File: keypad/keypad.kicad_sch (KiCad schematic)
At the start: 55 parts, among them P1 USB_C_Plug_USB2.0, SW1 SW_MEC_5E, SW2 SW_MEC_5E, SW3 SW_DIP_x01, SW4 SW_Push, SW5 SW_Push, SW6 SW_Push, U1 RP2040, U2 74HCT245, U3 W25Q16JVUXIQ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

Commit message: Finish RGB and start power
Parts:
- removed SW2: SW_MEC_5E, Button_Switch_THT:SW_Push_2P1T_Toggle_CK_PVA1xxH1xxxxxxV2, symbol Switch:SW_MEC_5E
- removed SW6: SW_Push, Button_Switch_Keyboard:SW_Cherry_MX_1.00u_PCB, symbol Switch:SW_Push
- removed U7: DRV5033AJxDBZ, Package_TO_SOT_SMD:SOT-23, symbol Sensor_Magnetic:DRV5033AJxDBZ
- added D7, D8, D9: WS2812B, LED_SMD:LED_WS2812B_PLCC4_5.0x5.0mm_P3.2mm, symbol LED:WS2812B
- added SW2: SW_MEC_5E, Button_Switch_SMD:SW_Push_1P1T_NO_6x6mm_H9.5mm, symbol Switch:SW_Push
- C3, C4: value 27 pF -> 10 pF
- SW1: footprint Button_Switch_THT:SW_Push_2P1T_Toggle_CK_PVA1xxH1xxxxxxV2 -> Button_Switch_SMD:SW_Push_1P1T_NO_6x6mm_H9.5mm; symbol Switch:SW_MEC_5E -> Switch:SW_Push
- SW3: footprint Button_Switch_SMD:SW_DIP_SPSTx01_Slide_9.78x4.72mm_W8.61mm_P2.54mm -> Jumper:SolderJumper-2_P1.3mm_Open_Pad1.0x1.5mm
- Y1: value ABLS-12.000MHz-B4-T -> ABM8G-12.000MHZ-4Y-T3; footprint Crystal:Crystal_HC18-U_Vertical -> Crystal:Crystal_SMD_Abracon_ABM8G-4Pin_3.2x2.5mm; symbol Device:Crystal -> Device:Crystal_GND24
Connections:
- net +3.3V: now also SW1.2, SW2.2; no longer C21.1, SW1.4 (A)
- net AUX0: now also U1.29 (GPIO18); no longer U1.6 (GPIO4)
- net AUX1: now also U1.30 (GPIO19); no longer U1.7 (GPIO5)
- net GND: now also Y1.2, Y1.4, D7.3 (VSS), D8.3 (VSS), D9.3 (VSS)
- net RGB_D0: now also U1.28 (GPIO17); no longer U1.12 (GPIO9)
- net VBUS: now also D7.1 (VDD), D8.1 (VDD), D9.1 (VDD)
- net at C5.1, C6.1, U1.23 (DVDD)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: now also C21.1
- net at C3.2, U1.20 (XIN): now also Y1.3; no longer Y1.2
- net at R2.2, R4.1: now also SW2.1
- net at D5.2 (DOUT): now also D7.4 (DIN)
- net ADC2: no longer names the net of U1.40 (GPIO28_ADC2)
- new net: D8.2 (DOUT), D9.4 (DIN)
- new net: D7.2 (DOUT), D8.4 (DIN)
- no-connect marks 51 -> 46
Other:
- moved on the sheet: C13, C15, C5, C6, C8, D1, D2, D3, D4, D5, SW4, SW5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

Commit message: finish placing everything
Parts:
- added C22: 100n, Capacitor_SMD:C_0805_2012Metric, symbol Device:C
- added J1: Conn_01x02_Male, Connector_PinHeader_1.27mm:PinHeader_1x02_P1.27mm_Vertical, symbol Connector:Conn_01x02_Male
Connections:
- net +3.3V: now also C22.1; no longer C7.1, U1.43 (ADC_AVDD)
- net ADC_AVDD: now also C7.1, U1.43 (ADC_AVDD)
- net GND: now also C22.2
- net at U1.24 (SWCLK): now also J1.1 (Pin_1)
- net at U1.25 (SWD): now also J1.2 (Pin_2)
- no-connect marks 46 -> 44
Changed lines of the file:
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@@
   (junction (at 185.42 233.68) (diameter 0) (color 0 0 0 0)
   )
+  (junction (at 203.2 53.34) (diameter 0) (color 0 0 0 0)
+  )
   (junction (at 107.95 71.12) (diameter 0) (color 0 0 0 0)
   )
@@
   )
   (junction (at 85.09 146.05) (diameter 0) (color 0 0 0 0)
-  )
-  (junction (at 151.13 63.5) (diameter 0) (color 0 0 0 0)
   )
   (junction (at 185.42 213.36) (diameter 0) (color 0 0 0 0)
@@
   (no_connect (at 125.73 218.44))
   (no_connect (at 377.19 212.09))
-  (no_connect (at 111.76 156.21))
   (no_connect (at 162.56 148.59))
   (no_connect (at 151.13 231.14))
@@
   (no_connect (at 162.56 110.49))
   (no_connect (at 382.27 212.09))
-  (no_connect (at 111.76 158.75))
   (no_connect (at 162.56 92.71))
   (no_connect (at 162.56 130.81))
@@
     (stroke (width 0) (type default) (color 0 0 0 0))
   )
+  (wire (pts (xy 104.14 162.56) (xy 106.68 162.56))
+    (stroke (width 0) (type default) (color 0 0 0 0))
+  )
   (wire (pts (xy 73.66 212.09) (xy 73.66 214.63))
     (stroke (width 0) (type default) (color 0 0 0 0))
@@
     (stroke (width 0) (type default) (color 0 0 0 0))
   )
+  (wire (pts (xy 203.2 53.34) (xy 217.17 53.34))
+    (stroke (width 0) (type default) (color 0 0 0 0))
+  )
   (wire (pts (xy 330.2 213.36) (xy 306.07 213.36))
     (stroke (width 0) (type default) (color 0 0 0 0))
@@
     (stroke (width 0) (type default) (color 0 0 0 0))
   )
+  (wire (pts (xy 106.68 162.56) (xy 106.68 158.75))
+    (stroke (width 0) (type default) (color 0 0 0 0))
+  )
   (wire (pts (xy 175.26 53.34) (xy 189.23 53.34))
     (stroke (width 0) (type default) (color 0 0 0 0))
@@
     (stroke (width 0) (type default) (color 0 0 0 0))
   )
+  (wire (pts (xy 104.14 156.21) (xy 111.76 156.21))
+    (stroke (width 0) (type default) (color 0 0 0 0))
+  )
   (wire (pts (xy 99.06 153.67) (xy 105.41 153.67))
     (stroke (width 0) (type default) (color 0 0 0 0))
@@
     (stroke (width 0) (type default) (color 0 0 0 0))
   )
+  (wire (pts (xy 106.68 158.75) (xy 111.76 158.75))
+    (stroke (width 0) (type default) (color 0 0 0 0))
+  )
   (wire (pts (xy 73.66 135.89) (xy 71.12 135.89))
     (stroke (width 0) (type default) (color 0 0 0 0))
@@
   )
   (wire (pts (xy 60.96 201.93) (xy 63.5 201.93))
+    (stroke (width 0) (type default) (color 0 0 0 0))
+  )
+  (wire (pts (xy 104.14 160.02) (xy 104.14 156.21))
     (stroke (width 0) (type default) (color 0 0 0 0))
   )
@@
     )
   )
+  (global_label "ADC_AVDD" (shape input) (at 144.78 63.5 90) (fields_autoplaced)
+    (effects (font (size 1.27 1.27)) (justify left))
+    (property "Intersheet References" "${INTERSHEET_REFS}" (id 0) (at 144.8594 51.7736 90)
+      (effects (font (size 1.27 1.27)) (justify left) hide)
+    )
+  )
   (global_label "QSPI_SD0" (shape input) (at 111.76 113.03 180) (fields_autoplaced)
     (effects (font (size 1.27 1.27)) (justify right))
@@
     )
     (pin "1")
+  )
+  (symbol (lib_id "Connector:Conn_01x02_Male") (at 99.06 160.02 0) (unit 1)
+    (in_bom yes) (on_board yes) (fields_autoplaced)
+    (property "Reference" "J1" (id 0) (at 99.695 154.94 0))
+    (property "Value" "Conn_01x02_Male" (id 1) (at 99.695 157.48 0))
+    (property "Footprint" "Connector_PinHeader_1.27mm:PinHeader_1x02_P1.27mm_Vertical" (id 2) (at 99.06 160.02 0)
+      (effects (font (size 1.27 1.27)) hide)
+    )
+    (property "Datasheet" "~" (id 3) (at 99.06 160.02 0)
+      (effects (font (size 1.27 1.27)) hide)
+    )
+    (pin "1")
+    (pin "2")
   )
   (symbol (lib_id "power:+3.3V") (at 95.25 201.93 0) (unit 1)
@@
     (pin "2")
   )
+  (symbol (lib_id "power:GND") (at 217.17 60.96 0) (unit 1)
+    (in_bom yes) (on_board yes) (fields_autoplaced)
+    (property "Reference" "#PWR0105" (id 0) (at 217.17 67.31 0)
+      (effects (font (size 1.27 1.27)) hide)
+    )
+    (property "Value" "GND" (id 1) (at 217.17 66.04 0))
+    (property "Footprint" "" (id 2) (at 217.17 60.96 0)
+      (effects (font (size 1.27 1.27)) hide)
+    )
+    (property "Datasheet" "" (id 3) (at 217.17 60.96 0)
+      (effects (font (size 1.27 1.27)) hide)
+    )
+    (pin "1")
+  )
   (symbol (lib_id "LED:WS2812B") (at 306.07 223.52 0) (unit 1)
     (in_bom yes) (on_board yes) (fields_autoplaced)
@@
     (pin "1")
     (pin "2")
-  )
-  (symbol (lib_id "power:+3.3V") (at 151.13 63.5 0) (unit 1)
-    (in_bom yes) (on_board yes) (fields_autoplaced)
-    (property "Reference" "#PWR011" (id 0) (at 151.13 67.31 0)
-      (effects (font (size 1.27 1.27)) hide)
-    )
-    (property "Value" "+3.3V" (id 1) (at 151.13 58.42 0))
-    (property "Footprint" "" (id 2) (at 151.13 63.5 0)
-      (effects (font (size 1.27 1.27)) hide)
-    )
-    (property "Datasheet" "" (id 3) (at 151.13 63.5 0)
-      (effects (font (size 1.27 1.27)) hide)
-    )
-    (pin "1")
   )
   (symbol (lib_id "power:VBUS") (at 153.67 196.85 0) (unit 1)
@@
     (pin "1")
   )
+  (symbol (lib_id "Device:C") (at 217.17 57.15 0) (unit 1)
+    (in_bom yes) (on_board yes) (fields_autoplaced)
+    (property "Reference" "C22" (id 0) (at 220.98 55.8799 0)
+      (effects (font (size 1.27 1.27)) (justify left))
+    )
+    (property "Value" "100n" (id 1) (at 220.98 58.4199 0)
+      (effects (font (size 1.27 1.27)) (justify left))
+    )
+    (property "Footprint" "Capacitor_SMD:C_0805_2012Metric" (id 2) (at 218.1352 60.96 0)
+      (effects (font (size 1.27 1.27)) hide)
+    )
+    (property "Datasheet" "~" (id 3) (at 217.17 57.15 0)
+      (effects (font (size 1.27 1.27)) hide)
+    )
+    (pin "1")
+    (pin "2")
+  )
   (symbol (lib_id "Memory_Flash:W25Q128JVS") (at 241.3 154.94 0) (unit 1)
     (in_bom yes) (on_board yes) (fields_autoplaced)
@@
       (reference "#PWR010") (unit 1) (value "GND") (footprint "")
     )
-    (path "/23cc3252-ed8c-45cf-a713-782ec5caed06"
-      (reference "#PWR011") (unit 1) (value "+3.3V") (footprint "")
-    )
     (path "/8eb3de26-1785-4ce6-9eea-d7c5a25d46d7"
       (reference "#PWR012") (unit 1) (value "GND") (footprint "")
@@
       (reference "#PWR0104") (unit 1) (value "+3.3V") (footprint "")
     )
+    (path "/15c1f430-c43e-49de-8952-ebfdd7bc920c"
+      (reference "#PWR0105") (unit 1) (value "GND") (footprint "")
+    )
     (path "/34b4b529-e4df-4286-a018-6816c646e656"
       (reference "C1") (unit 1) (value "10u") (footprint "Capacitor_SMD:C_0805_2012Metric")
@@
       (reference "C21") (unit 1) (value "100n") (footprint "Capacitor_SMD:C_0805_2012Metric")
     )
+    (path "/de4da200-f592-40f0-ab93-f2fa8fe75a9d"
+      (reference "C22") (unit 1) (value "100n") (footprint "Capacitor_SMD:C_0805_2012Metric")
+    )
     (path "/6a00ced7-1c3c-4889-9134-cc26d1227900"
       (reference "D1") (unit 1) (value "WS2812B") (footprint "LED_SMD:LED_WS2812B_PLCC4_5.0x5.0mm_P3.2mm")
@@
       (reference "D9") (unit 1) (value "WS2812B") (footprint "LED_SMD:LED_WS2812B_PLCC4_5.0x5.0mm_P3.2mm")
     )
+    (path "/02de3128-fb16-4162-a5b1-0ab2657c91ec"
+      (reference "J1") (unit 1) (value "Conn_01x02_Male") (footprint "Connector_PinHeader_1.27mm:PinHeader_1x02_P1.27mm_Vertical")
+    )
     (path "/e71c45d6-c81d-4298-b2c4-54f273ae81a6"

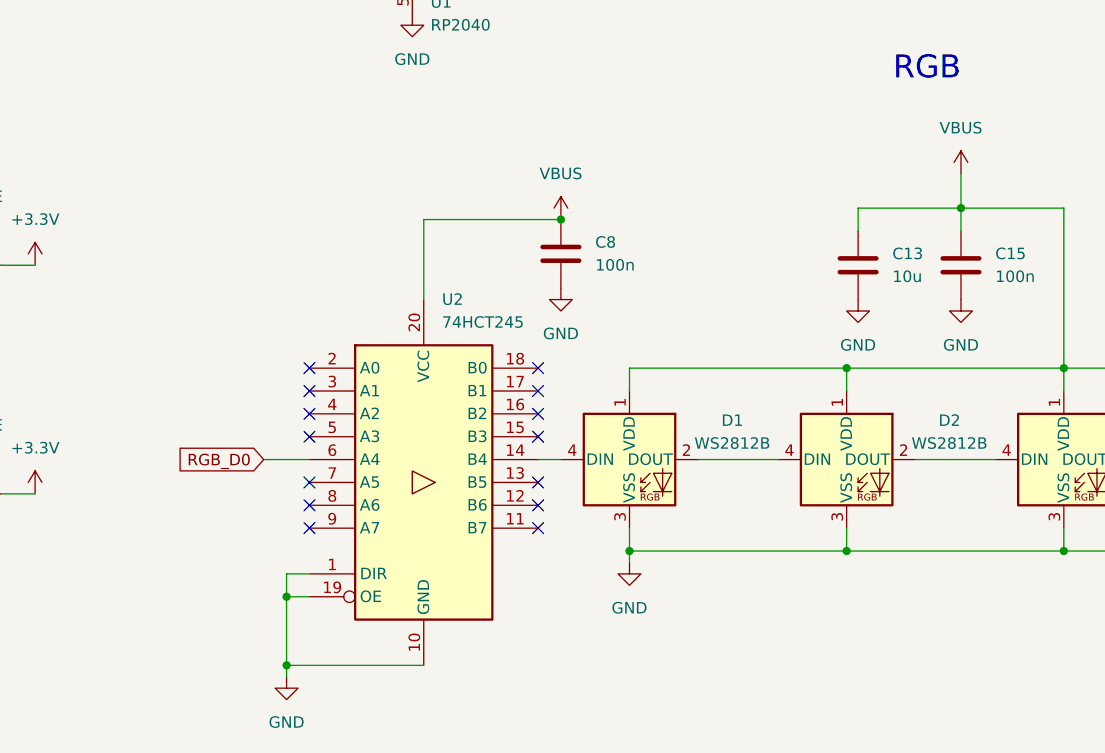
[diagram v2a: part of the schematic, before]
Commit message: Rewire RGB to add space for screwholes
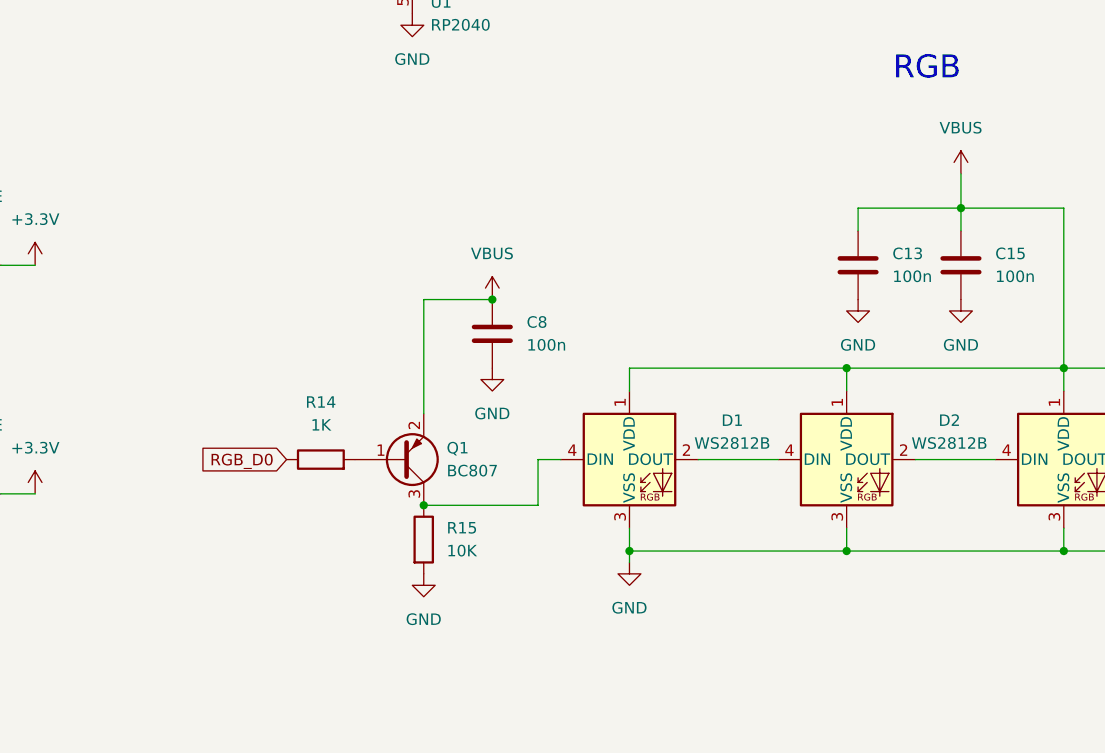
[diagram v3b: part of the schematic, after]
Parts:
- removed U2: 74HCT245, Package_SO:TSSOP-20_4.4x6.5mm_P0.65mm, symbol Custom_Parts:74HCT245
- added Q1: BC807, Package_TO_SOT_SMD:SOT-23, symbol Transistor_BJT:BC807
- added R14: 1K, Resistor_SMD:R_0805_2012Metric, symbol Device:R
- added R15: 10K, Resistor_SMD:R_0805_2012Metric, symbol Device:R
- C13: value 10u -> 100n
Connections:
- net GND: now also R15.2
- net RGB_D0: now also R14.1
- net VBUS: now also Q1.2 (E)
- net at D1.4 (DIN): now also Q1.3 (C), R15.1
- new net: Q1.1 (B), R14.2
- no-connect marks 44 -> 30
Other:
- moved on the sheet: C8

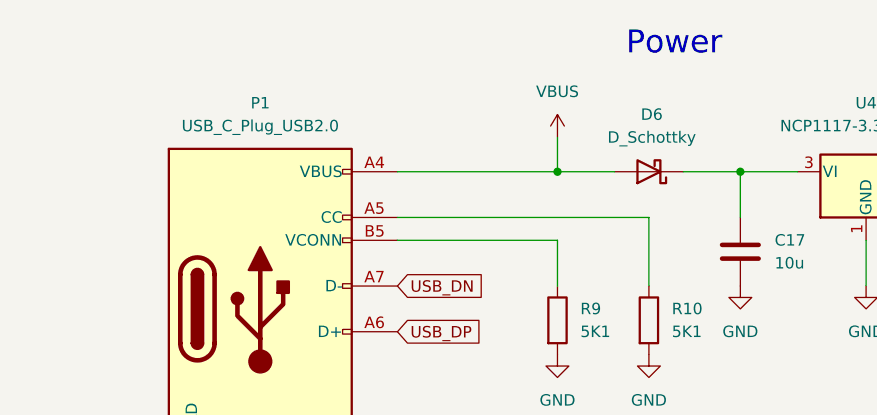
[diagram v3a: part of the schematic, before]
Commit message: Re-spec USB-C and power diode
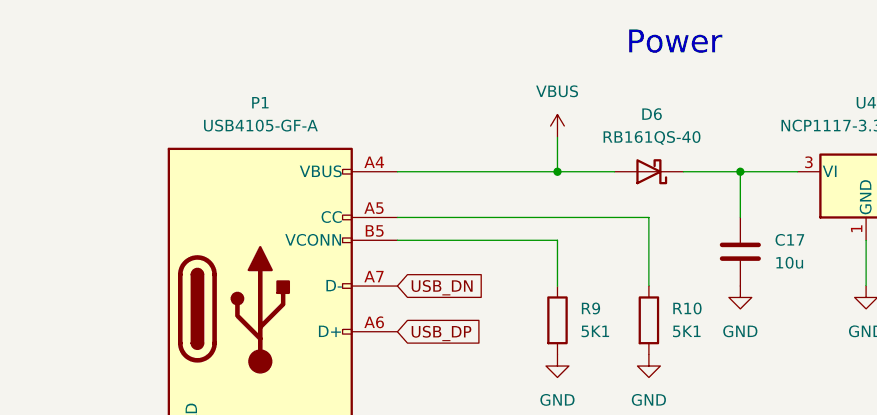
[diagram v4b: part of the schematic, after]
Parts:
- D6: value D_Schottky -> RB161QS-40; footprint Diode_SMD:D_1812_4532Metric -> Diode_SMD:D_0402_1005Metric
- P1: value USB_C_Plug_USB2.0 -> USB4105-GF-A; footprint Connector_USB:USB_C_Receptacle_CNCTech_C-ARA1-AK51X -> Connector_USB:USB_C_Receptacle_GCT_USB4105-xx-A_16P_TopMnt_Horizontal
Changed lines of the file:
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@@
     (in_bom yes) (on_board yes) (fields_autoplaced)
     (property "Reference" "D6" (id 0) (at 300.0375 43.18 0))
-    (property "Value" "D_Schottky" (id 1) (at 300.0375 45.72 0))
-    (property "Footprint" "Diode_SMD:D_1812_4532Metric" (id 2) (at 299.72 49.53 0)
+    (property "Value" "RB161QS-40" (id 1) (at 300.0375 45.72 0))
+    (property "Footprint" "Diode_SMD:D_0402_1005Metric" (id 2) (at 299.72 49.53 0)
       (effects (font (size 1.27 1.27)) hide)
     )
@@
     (in_bom yes) (on_board yes) (fields_autoplaced)
     (property "Reference" "P1" (id 0) (at 256.54 41.91 0))
-    (property "Value" "USB_C_Plug_USB2.0" (id 1) (at 256.54 44.45 0))
-    (property "Footprint" "Connector_USB:USB_C_Receptacle_CNCTech_C-ARA1-AK51X" (id 2) (at 260.35 64.77 0)
+    (property "Value" "USB4105-GF-A" (id 1) (at 256.54 44.45 0))
+    (property "Footprint" "Connector_USB:USB_C_Receptacle_GCT_USB4105-xx-A_16P_TopMnt_Horizontal" (id 2) (at 260.35 64.77 0)
       (effects (font (size 1.27 1.27)) hide)
     )
@@
     )
     (path "/351311bb-3268-4bcb-bbf4-ddc178223b1f"
-      (reference "D6") (unit 1) (value "D_Schottky") (footprint "Diode_SMD:D_1812_4532Metric")
+      (reference "D6") (unit 1) (value "RB161QS-40") (footprint "Diode_SMD:D_0402_1005Metric")
     )
     (path "/7bcdada4-b9e5-4f91-9f48-909e88f9fc6f"
@@
     )
     (path "/e71c45d6-c81d-4298-b2c4-54f273ae81a6"
-      (reference "P1") (unit 1) (value "USB_C_Plug_USB2.0") (footprint "Connector_USB:USB_C_Receptacle_CNCTech_C-ARA1-AK51X")
+      (reference "P1") (unit 1) (value "USB4105-GF-A") (footprint "Connector_USB:USB_C_Receptacle_GCT_USB4105-xx-A_16P_TopMnt_Horizontal")
     )
     (path "/f3858d36-0e5f-477a-81b2-f2f3059a6f61"

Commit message: Minor updates, prep for fab
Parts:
- removed C1, C2: 10u, Capacitor_SMD:C_0805_2012Metric, symbol Device:C
- removed R1, R2: 100R, Resistor_SMD:R_0805_2012Metric, symbol Device:R
- D1, D2, D3, D4, D5, D7, D8, D9: value WS2812B -> WS2812B-B/T
- J1: value Conn_01x02_Male -> NO FIT
- Q1: value BC807 -> BC807-40LT1G
- SW1, SW2: value SW_MEC_5E -> TS04-66-70-BK-100-SMT
- SW3: value SW_DIP_x01 -> NO FIT
- SW4, SW5: value SW_Push -> NO FIT
- U3: value W25Q16JVUXIQ -> W25Q16JVSSIQ
- U5, U6: value DRV5033AJxDBZ -> DRV5053VAQDBZR
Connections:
- net AUX0: now also R3.1, SW1.1
- net AUX1: now also R4.1, SW2.1

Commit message: fix mistakes because i am big dum
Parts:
- C3, C4: value 10 pF -> 2p
- P1: value USB4105-GF-A -> GT-USB-7010ASV; footprint Connector_USB:USB_C_Receptacle_GCT_USB4105-xx-A_16P_TopMnt_Horizontal -> Connector_USB:USB_C_Receptacle_G-Switch_GT-USB-7010ASV
- Y1: value ABM8G-12.000MHZ-4Y-T3 -> NX3225SA-12MHz-STD-CSR-6; footprint Crystal:Crystal_SMD_Abracon_ABM8G-4Pin_3.2x2.5mm -> Custom_Footprints:Crystal_SMD_NX3225SA
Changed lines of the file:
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@@
     (in_bom yes) (on_board yes)
     (property "Reference" "C4" (id 0) (at 77.47 151.13 90))
-    (property "Value" "10 pF" (id 1) (at 77.47 153.67 90))
+    (property "Value" "2p" (id 1) (at 77.47 153.67 90))
     (property "Footprint" "Capacitor_SMD:C_0805_2012Metric" (id 2) (at 81.28 145.0848 0)
       (effects (font (size 1.27 1.27)) hide)
@@
     (in_bom yes) (on_board yes) (fields_autoplaced)
     (property "Reference" "C3" (id 0) (at 77.47 128.27 90))
-    (property "Value" "10 pF" (id 1) (at 77.47 130.81 90))
+    (property "Value" "2p" (id 1) (at 77.47 130.81 90))
     (property "Footprint" "Capacitor_SMD:C_0805_2012Metric" (id 2) (at 81.28 134.9248 0)
       (effects (font (size 1.27 1.27)) hide)
@@
       (effects (font (size 1.27 1.27)) (justify right))
     )
-    (property "Value" "ABM8G-12.000MHZ-4Y-T3" (id 1) (at 88.9 142.2399 90)
+    (property "Value" "NX3225SA-12MHz-STD-CSR-6" (id 1) (at 88.9 142.2399 90)
       (effects (font (size 1.27 1.27)) (justify right))
     )
-    (property "Footprint" "Crystal:Crystal_SMD_Abracon_ABM8G-4Pin_3.2x2.5mm" (id 2) (at 85.09 140.97 0)
+    (property "Footprint" "Custom_Footprints:Crystal_SMD_NX3225SA" (id 2) (at 85.09 140.97 0)
       (effects (font (size 1.27 1.27)) hide)
     )
@@
     (in_bom yes) (on_board yes) (fields_autoplaced)
     (property "Reference" "P1" (id 0) (at 256.54 41.91 0))
-    (property "Value" "USB4105-GF-A" (id 1) (at 256.54 44.45 0))
-    (property "Footprint" "Connector_USB:USB_C_Receptacle_GCT_USB4105-xx-A_16P_TopMnt_Horizontal" (id 2) (at 260.35 64.77 0)
+    (property "Value" "GT-USB-7010ASV" (id 1) (at 256.54 44.45 0))
+    (property "Footprint" "Connector_USB:USB_C_Receptacle_G-Switch_GT-USB-7010ASV" (id 2) (at 260.35 64.77 0)
       (effects (font (size 1.27 1.27)) hide)
     )
@@
     )
     (path "/4dc74779-8a31-4965-91a2-f7be2910fea6"
-      (reference "C3") (unit 1) (value "10 pF") (footprint "Capacitor_SMD:C_0805_2012Metric")
+      (reference "C3") (unit 1) (value "2p") (footprint "Capacitor_SMD:C_0805_2012Metric")
     )
     (path "/1501d357-9863-4281-a95e-61a179bf8ce1"
-      (reference "C4") (unit 1) (value "10 pF") (footprint "Capacitor_SMD:C_0805_2012Metric")
+      (reference "C4") (unit 1) (value "2p") (footprint "Capacitor_SMD:C_0805_2012Metric")
     )
     (path "/39116b8e-8ab9-4568-a2f6-d373c53f4da8"
@@
     )
     (path "/e71c45d6-c81d-4298-b2c4-54f273ae81a6"
-      (reference "P1") (unit 1) (value "USB4105-GF-A") (footprint "Connector_USB:USB_C_Receptacle_GCT_USB4105-xx-A_16P_TopMnt_Horizontal")
+      (reference "P1") (unit 1) (value "GT-USB-7010ASV") (footprint "Connector_USB:USB_C_Receptacle_G-Switch_GT-USB-7010ASV")
     )
     (path "/f3858d36-0e5f-477a-81b2-f2f3059a6f61"
@@
     )
     (path "/87608c5f-2ede-4c25-bcfc-bda360d43b90"
-      (reference "Y1") (unit 1) (value "ABM8G-12.000MHZ-4Y-T3") (footprint "Crystal:Crystal_SMD_Abracon_ABM8G-4Pin_3.2x2.5mm")
-    )
-  )
+      (reference "Y1") (unit 1) (value "NX3225SA-12MHz-STD-CSR-6") (footprint "Custom_Footprints:Crystal_SMD_NX3225SA")
+    )
+  )

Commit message: Make alterations for rev3
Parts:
- removed J1: NO FIT, Connector_PinHeader_1.27mm:PinHeader_1x02_P1.27mm_Vertical, symbol Connector:Conn_01x02_Male
- removed SW3: NO FIT, Jumper:SolderJumper-2_P1.3mm_Open_Pad1.0x1.5mm, symbol Switch:SW_DIP_x01
- added C1, C2: 100n, Capacitor_SMD:C_0805_2012Metric, symbol Device:C
- added C23: 47u, Capacitor_SMD:C_0805_2012Metric, symbol Device:C
- added C24, C25: 1n5, Capacitor_SMD:C_0805_2012Metric, symbol Device:C
- added D10: SMLP14ECNWT86, LED_SMD:LED_0603_1608Metric, symbol Device:LED
- added J1, J2: NO FIT, Connector_PinSocket_2.00mm:PinSocket_1x02_P2.00mm_Vertical, symbol Connector:Conn_01x02_Female
- added R1: 1R, Resistor_SMD:R_0805_2012Metric, symbol Device:R
- added R2: 200R, Resistor_SMD:R_0805_2012Metric, symbol Device:R
- added TP1, TP2: NO FIT, TestPoint:TestPoint_Pad_1.5x1.5mm, symbol Connector:TestPoint
- added U2: LM4040DBZ-2.0, Package_TO_SOT_SMD:SOT-23, symbol Reference_Voltage:LM4040DBZ-2.0
- C10, C5, C7: value 1u -> 2u2
- C17, C18: value 10u -> 47u
- R11, R12: value 27R -> 10K
- R13, R5, R6, R7: Tolerance (none) -> 1%
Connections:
- net +3.3V: now also D10.2 (A), R2.2; no longer R11.1
- net ADC0: now also R11.2, TP1.1; no longer U5.2 (OUT)
- net ADC1: now also R12.2, TP2.1; no longer U6.2 (OUT)
- net ADC_AVDD: now also R1.1; no longer R11.2, R12.1
- net GND: now also C1.2, C2.2, C23.2, C24.2, C25.2, J2.1 (Pin_1), U2.1 (K)
- net VBUS: now also C1.1, C2.1, C23.1
- net at U1.24 (SWCLK): now also J1.2 (Pin_2)
- net at U1.25 (SWD): now also J1.1 (Pin_1)
- net at R8.1: now also J2.2 (Pin_2)
- net at R13.1: now also D10.1 (K); no longer R12.2
- new net: C25.1, R12.1, U6.2 (OUT)
- new net: C24.1, R11.1, U5.2 (OUT)
- new net: R1.2, R2.1, U2.2 (A)
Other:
- moved on the sheet: C13, C15, C17, C18, C19, C20, D6, R10, R4, R9, SW2, U4
